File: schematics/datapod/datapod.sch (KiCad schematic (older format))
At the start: 5 parts, among them U1 ATmega328P-PU, Y1 16Mhz

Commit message: made 1st pcb
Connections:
- net VcR1: no longer names the net of RN1.10 (R10.1)
- no-connect marks 5 -> 6
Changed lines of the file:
@@
 Wire Wire Line
 	4200 6700 4550 6700
-Text GLabel 3600 6700 0    50   Input ~ 0
-VcR1
-Wire Wire Line
-	3600 6700 3800 6700
 Text GLabel 2450 1550 2    50   Input ~ 0
 MICRO_SD_CS
@@
 Connection ~ 4550 5900
 Connection ~ 4550 6000
+NoConn ~ 3800 6700
 $EndSCHEMATC

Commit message: added final routed PCB, gerbers and BOM
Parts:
- C1, C2: Part# (none) -> GJM0335C1HR22WB01D; part# GJM0335C1HR22WB01D -> (none)
- U1: Part# (none) -> 110-47-328-41-105000; Value2 110-47-328-41-105000 -> (none); Vendor microchip -> Digikey
- Y1: Part# (none) -> SER3686DKR-ND; part# SER3686DKR-ND -> (none)
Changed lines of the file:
@@
 F 2 "Package_DIP:DIP-28_W7.62mm_SMDSocket_SmallPads" H 1600 2550 50  0001 C CIN
 F 3 "http://ww1.microchip.com/downloads/en/DeviceDoc/ATmega328_P%20AVR%20MCU%20with%20picoPower%20Technology%20Data%20Sheet%2040001984A.pdf" H 1600 2550 50  0001 C CNN
-F 4 "microchip" H 1600 2550 50  0001 C CNN "Vendor"
-F 5 "110-47-328-41-105000 " H 1600 2550 50  0001 C CNN "Value2"
+F 4 "Digikey" H 1600 2550 50  0001 C CNN "Vendor"
+F 5 "110-47-328-41-105000 " H 1600 2550 50  0001 C CNN "Part#"
 F 6 "https://www.digikey.com/products/en?mpart=110-47-328-41-105000&v=54" H 1600 2550 50  0001 C CNN "Datasheet2"
 	1    1600 2550
@@
 F 4 "Digikey" H 4200 2150 50  0001 C CNN "Vendor"
 F 5 "https://www.digikey.com/product-detail/en/epson/FA-238-16.0000MB-C3/SER3686DKR-ND/2403540" H 4200 2150 50  0001 C CNN "extra"
-F 6 "SER3686DKR-ND" H 4200 2150 50  0001 C CNN "part#"
+F 6 "SER3686DKR-ND" H 4200 2150 50  0001 C CNN "Part#"
 	1    4200 2150
 	0    -1   -1   0
@@
 F 3 "https://search.murata.co.jp/Ceramy/image/img/A01X/G101/ENG/GJM0335C1HR22WB01-01.pdf" H 4200 1550 50  0001 C CNN
 F 4 "Digikey" H 4200 1550 50  0001 C CNN "Vendor"
-F 5 " GJM0335C1HR22WB01D" H 4200 1550 50  0001 C CNN "part#"
+F 5 " GJM0335C1HR22WB01D" H 4200 1550 50  0001 C CNN "Part#"
 	1    4200 1550
 	1    0    0    -1
@@
 F 3 "https://search.murata.co.jp/Ceramy/image/img/A01X/G101/ENG/GJM0335C1HR22WB01-01.pdf" H 4200 2750 50  0001 C CNN
 F 4 "Digikey" H 4200 2750 50  0001 C CNN "Vendor"
-F 5 " GJM0335C1HR22WB01D" H 4200 2750 50  0001 C CNN "part#"
+F 5 " GJM0335C1HR22WB01D" H 4200 2750 50  0001 C CNN "Part#"
 	1    4200 2750
 	1    0    0    -1

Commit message: restored lost changes... moving sd card reader and replacing rn2 with actual resistors
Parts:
- C1, C2: footprint Capacitor_SMD:C_0201_0603Metric -> Capacitor_SMD:C_1206_3216Metric_Pad1.42x1.75mm_HandSolder; Part# GJM0335C1HR22WB01D -> (none); part# (none) -> 399-9326-1-ND
- U1: symbol MCU_Microchip_ATmega:ATmega328P-PU -> datapod-rescue:ATmega328P-PU-MCU_Microchip_ATmega; Part# 110-47-328-41-105000 -> (none); Value2 (none) -> 110-47-328-41-105000; Vendor Digikey -> microchip
- Y1: Part# SER3686DKR-ND -> (none); part# (none) -> SER3686DKR-ND
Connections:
- net VcR1: now reaches RN1.10 (R10.1)
- no-connect marks 6 -> 5
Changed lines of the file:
@@
 EESchema Schematic File Version 4
-LIBS:datapod-cache
 EELAYER 30 0
 EELAYER END
@@
 $EndDescr
 $Comp
-L MCU_Microchip_ATmega:ATmega328P-PU U1
+L datapod-rescue:ATmega328P-PU-MCU_Microchip_ATmega U1
 U 1 1 5DBAFE2C
 P 1600 2550
@@
 F 2 "Package_DIP:DIP-28_W7.62mm_SMDSocket_SmallPads" H 1600 2550 50  0001 C CIN
 F 3 "http://ww1.microchip.com/downloads/en/DeviceDoc/ATmega328_P%20AVR%20MCU%20with%20picoPower%20Technology%20Data%20Sheet%2040001984A.pdf" H 1600 2550 50  0001 C CNN
-F 4 "Digikey" H 1600 2550 50  0001 C CNN "Vendor"
-F 5 "110-47-328-41-105000 " H 1600 2550 50  0001 C CNN "Part#"
+F 4 "microchip" H 1600 2550 50  0001 C CNN "Vendor"
+F 5 "110-47-328-41-105000 " H 1600 2550 50  0001 C CNN "Value2"
 F 6 "https://www.digikey.com/products/en?mpart=110-47-328-41-105000&v=54" H 1600 2550 50  0001 C CNN "Datasheet2"
 	1    1600 2550
@@
 F 4 "Digikey" H 4200 2150 50  0001 C CNN "Vendor"
 F 5 "https://www.digikey.com/product-detail/en/epson/FA-238-16.0000MB-C3/SER3686DKR-ND/2403540" H 4200 2150 50  0001 C CNN "extra"
-F 6 "SER3686DKR-ND" H 4200 2150 50  0001 C CNN "Part#"
+F 6 "SER3686DKR-ND" H 4200 2150 50  0001 C CNN "part#"
 	1    4200 2150
 	0    -1   -1   0
@@
 F 0 "C1" H 4300 1800 50  0000 L CNN
 F 1 "20pF" H 4300 1700 50  0000 L CNN
-F 2 "Capacitor_SMD:C_0201_0603Metric" H 4238 1400 50  0001 C CNN
-F 3 "https://search.murata.co.jp/Ceramy/image/img/A01X/G101/ENG/GJM0335C1HR22WB01-01.pdf" H 4200 1550 50  0001 C CNN
+F 2 "Capacitor_SMD:C_1206_3216Metric_Pad1.42x1.75mm_HandSolder" H 4238 1400 50  0001 C CNN
+F 3 "https://api.kemet.com/component-edge/download/datasheet/C1206C200K5GACTU.pdf" H 4200 1550 50  0001 C CNN
 F 4 "Digikey" H 4200 1550 50  0001 C CNN "Vendor"
-F 5 " GJM0335C1HR22WB01D" H 4200 1550 50  0001 C CNN "Part#"
+F 5 "399-9326-1-ND" H 4200 1550 50  0001 C CNN "part#"
 	1    4200 1550
-	1    0    0    -1
-$EndComp
-$Comp
-L Device:C C2
-U 1 1 5DBE647B
-P 4200 2750
-F 0 "C2" H 4315 2796 50  0000 L CNN
-F 1 "20pF" H 4315 2705 50  0000 L CNN
-F 2 "Capacitor_SMD:C_0201_0603Metric" H 4238 2600 50  0001 C CNN
-F 3 "https://search.murata.co.jp/Ceramy/image/img/A01X/G101/ENG/GJM0335C1HR22WB01-01.pdf" H 4200 2750 50  0001 C CNN
-F 4 "Digikey" H 4200 2750 50  0001 C CNN "Vendor"
-F 5 " GJM0335C1HR22WB01D" H 4200 2750 50  0001 C CNN "Part#"
-	1    4200 2750
 	1    0    0    -1
 $EndComp
@@
 $EndComp
 $Comp
-L power:GND #PWR03
+L power:GND #PWR0101
 U 1 1 5DC66802
 P 3850 2150
-F 0 "#PWR03" H 3850 1900 50  0001 C CNN
+F 0 "#PWR0101" H 3850 1900 50  0001 C CNN
 F 1 "GND" H 3855 1977 50  0000 C CNN
 F 2 "" H 3850 2150 50  0001 C CNN
@@
 $EndComp
 $Comp
-L power:GND #PWR04
+L power:GND #PWR0102
 U 1 1 5DC67152
 P 4600 2150
-F 0 "#PWR04" H 4600 1900 50  0001 C CNN
+F 0 "#PWR0102" H 4600 1900 50  0001 C CNN
 F 1 "GND" H 4605 1977 50  0000 C CNN
 F 2 "" H 4600 2150 50  0001 C CNN
@@
 	4000 2150 3850 2150
 $Comp
-L power:GND #PWR05
+L power:GND #PWR0103
 U 1 1 5DC89AE2
 P 4200 3050
-F 0 "#PWR05" H 4200 2800 50  0001 C CNN
+F 0 "#PWR0103" H 4200 2800 50  0001 C CNN
 F 1 "GND" H 4205 2877 50  0000 C CNN
 F 2 "" H 4200 3050 50  0001 C CNN
@@
 $EndComp
 $Comp
-L power:GND #PWR02
+L power:GND #PWR0104
 U 1 1 5DC8A1B9
 P 3950 1400
-F 0 "#PWR02" H 3950 1150 50  0001 C CNN
+F 0 "#PWR0104" H 3950 1150 50  0001 C CNN
 F 1 "GND" H 3955 1227 50  0000 C CNN
 F 2 "" H 3950 1400 50  0001 C CNN
@@
 Connection ~ 4200 1700
 $Comp
-L power:GND #PWR08
+L power:GND #PWR0105
 U 1 1 5DCB2EF6
 P 4550 6750
-F 0 "#PWR08" H 4550 6500 50  0001 C CNN
+F 0 "#PWR0105" H 4550 6500 50  0001 C CNN
 F 1 "GND" H 4555 6577 50  0000 C CNN
 F 2 "" H 4550 6750 50  0001 C CNN
@@
 	4200 6000 4550 6000
 $Comp
-L power:+5V #PWR07
+L power:+5V #PWR0106
 U 1 1 5DCB93CE
 P 4550 5550
-F 0 "#PWR07" H 4550 5400 50  0001 C CNN
+F 0 "#PWR0106" H 4550 5400 50  0001 C CNN
 F 1 "+5V" H 4565 5723 50  0000 C CNN
 F 2 "" H 4550 5550 50  0001 C CNN
@@
 Connection ~ 4550 5800
 $Comp
-L power:+5V #PWR01
+L power:+5V #PWR0107
 U 1 1 5DC99875
 P 1650 900
-F 0 "#PWR01" H 1650 750 50  0001 C CNN
+F 0 "#PWR0107" H 1650 750 50  0001 C CNN
 F 1 "+5V" H 1665 1073 50  0000 C CNN
 F 2 "" H 1650 900 50  0001 C CNN
@@
 	1650 1050 1700 1050
 $Comp
-L power:GND #PWR06
+L power:GND #PWR0108
 U 1 1 5DCA0B51
 P 1600 4050
-F 0 "#PWR06" H 1600 3800 50  0001 C CNN
+F 0 "#PWR0108" H 1600 3800 50  0001 C CNN
 F 1 "GND" H 1605 3877 50  0000 C CNN
 F 2 "" H 1600 4050 50  0001 C CNN
@@
 Wire Wire Line
 	3550 1700 4200 1700
-Connection ~ 4200 2600
 Wire Wire Line
 	2200 2050 3550 2050
@@
 Wire Wire Line
 	4200 6700 4550 6700
+Text GLabel 3600 6700 0    50   Input ~ 0
+VcR1
+Wire Wire Line
+	3600 6700 3800 6700
 Text GLabel 2450 1550 2    50   Input ~ 0
 MICRO_SD_CS
@@
 Connection ~ 4550 5900
 Connection ~ 4550 6000
-NoConn ~ 3800 6700
+$Comp
+L Device:C C2
+U 1 1 5DDB6B24
+P 4200 2750
+F 0 "C2" H 4300 3000 50  0000 L CNN
+F 1 "20pF" H 4300 2900 50  0000 L CNN
+F 2 "Capacitor_SMD:C_1206_3216Metric_Pad1.42x1.75mm_HandSolder" H 4238 2600 50  0001 C CNN
+F 3 "https://api.kemet.com/component-edge/download/datasheet/C1206C200K5GACTU.pdf" H 4200 2750 50  0001 C CNN
+F 4 "Digikey" H 4200 2750 50  0001 C CNN "Vendor"
+F 5 "399-9326-1-ND" H 4200 2750 50  0001 C CNN "part#"
+	1    4200 2750
+	1    0    0    -1
+$EndComp
+Connection ~ 4200 2600
 $EndSCHEMATC

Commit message: fixed bad gnd trace on 3.3v circuit and added comments to the silkscreen
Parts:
- added H1: MountingHole, datapod:MountingHole_0.4_inches_Pad_Via, symbol Mechanical:MountingHole
- added J9: Conn_02x03_Odd_Even, Connector_PinHeader_2.54mm:PinHeader_2x03_P2.54mm_Vertical_SMD, symbol Connector_Generic:Conn_02x03_Odd_Even
- added TP2: TestPoint_2Pole, TestPoint:TestPoint_2Pads_Pitch5.08mm_Drill1.3mm, symbol Connector:TestPoint_2Pole
- C1, C2: value 20pF -> 22pF; part# 399-9326-1-ND -> 399-8165-1-ND
- U1: symbol datapod-rescue:ATmega328P-PU-MCU_Microchip_ATmega -> MCU_Microchip_ATmega:ATmega328P-PU
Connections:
- net +5V: now also J9.2 (Pin_2)
- net GND: now also J9.6 (Pin_6), TP2.1, TP2.2
- net MICRO_SD_MISO: now also J9.1 (Pin_1)
- net MICRO_SD_MOSI: now also J9.4 (Pin_4)
- net MICRO_SD_SCK: now also J9.3 (Pin_3)
- net ~RESET: now also J9.5 (Pin_5)
- net VcR1: no longer names the net of RN1.10 (R10.1)
- no-connect marks 5 -> 6
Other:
- note added: "ICSP"
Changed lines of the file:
@@
 $EndDescr
-$Comp
-L datapod-rescue:ATmega328P-PU-MCU_Microchip_ATmega U1
-U 1 1 5DBAFE2C
-P 1600 2550
-F 0 "U1" H 1000 4500 50  0000 R CNN
-F 1 "ATmega328P-PU" H 1300 4300 50  0000 R CNN
-F 2 "Package_DIP:DIP-28_W7.62mm_SMDSocket_SmallPads" H 1600 2550 50  0001 C CIN
-F 3 "http://ww1.microchip.com/downloads/en/DeviceDoc/ATmega328_P%20AVR%20MCU%20with%20picoPower%20Technology%20Data%20Sheet%2040001984A.pdf" H 1600 2550 50  0001 C CNN
-F 4 "microchip" H 1600 2550 50  0001 C CNN "Vendor"
-F 5 "110-47-328-41-105000 " H 1600 2550 50  0001 C CNN "Value2"
-F 6 "https://www.digikey.com/products/en?mpart=110-47-328-41-105000&v=54" H 1600 2550 50  0001 C CNN "Datasheet2"
-	1    1600 2550
-	1    0    0    -1
-$EndComp
 $Comp
 L Device:Crystal_GND24 Y1
@@
 P 4200 1550
 F 0 "C1" H 4300 1800 50  0000 L CNN
-F 1 "20pF" H 4300 1700 50  0000 L CNN
+F 1 "22pF" H 4300 1700 50  0000 L CNN
 F 2 "Capacitor_SMD:C_1206_3216Metric_Pad1.42x1.75mm_HandSolder" H 4238 1400 50  0001 C CNN
-F 3 "https://api.kemet.com/component-edge/download/datasheet/C1206C200K5GACTU.pdf" H 4200 1550 50  0001 C CNN
+F 3 "https://api.kemet.com/component-edge/download/datasheet/C1206C220K2GACTU.pdf" H 4200 1550 50  0001 C CNN
 F 4 "Digikey" H 4200 1550 50  0001 C CNN "Vendor"
-F 5 "399-9326-1-ND" H 4200 1550 50  0001 C CNN "part#"
+F 5 "399-8165-1-ND" H 4200 1550 50  0001 C CNN "part#"
 	1    4200 1550
 	1    0    0    -1
@@
 	1    0    0    -1
 $EndComp
-Wire Wire Line
-	1600 1050 1650 1050
-Wire Wire Line
-	1650 900  1650 1050
-Connection ~ 1650 1050
-Wire Wire Line
-	1650 1050 1700 1050
 $Comp
 L power:GND #PWR0108
@@
 Wire Wire Line
 	4200 6700 4550 6700
-Text GLabel 3600 6700 0    50   Input ~ 0
-VcR1
-Wire Wire Line
-	3600 6700 3800 6700
 Text GLabel 2450 1550 2    50   Input ~ 0
 MICRO_SD_CS
@@
 P 4200 2750
 F 0 "C2" H 4300 3000 50  0000 L CNN
-F 1 "20pF" H 4300 2900 50  0000 L CNN
+F 1 "22pF" H 4300 2900 50  0000 L CNN
 F 2 "Capacitor_SMD:C_1206_3216Metric_Pad1.42x1.75mm_HandSolder" H 4238 2600 50  0001 C CNN
-F 3 "https://api.kemet.com/component-edge/download/datasheet/C1206C200K5GACTU.pdf" H 4200 2750 50  0001 C CNN
+F 3 "https://api.kemet.com/component-edge/download/datasheet/C1206C220K2GACTU.pdf" H 4200 2750 50  0001 C CNN
 F 4 "Digikey" H 4200 2750 50  0001 C CNN "Vendor"
-F 5 "399-9326-1-ND" H 4200 2750 50  0001 C CNN "part#"
+F 5 "399-8165-1-ND" H 4200 2750 50  0001 C CNN "part#"
 	1    4200 2750
 	1    0    0    -1
 $EndComp
 Connection ~ 4200 2600
+NoConn ~ 3800 6700
+$Comp
+L Mechanical:MountingHole H1
+U 1 1 5E1EDB2E
+P 3100 4800
+F 0 "H1" H 3200 4846 50  0000 L CNN
+F 1 "MountingHole" H 3200 4755 50  0000 L CNN
+F 2 "datapod:MountingHole_0.4_inches_Pad_Via" H 3100 4800 50  0001 C CNN
+F 3 "~" H 3100 4800 50  0001 C CNN
+	1    3100 4800
+	1    0    0    -1
+$EndComp
+$Comp
+L MCU_Microchip_ATmega:ATmega328P-PU U1
+U 1 1 5DBAFE2C
+P 1600 2550
+F 0 "U1" H 1000 4500 50  0000 R CNN
+F 1 "ATmega328P-PU" H 1300 4300 50  0000 R CNN
+F 2 "Package_DIP:DIP-28_W7.62mm_SMDSocket_SmallPads" H 1600 2550 50  0001 C CIN
+F 3 "http://ww1.microchip.com/downloads/en/DeviceDoc/ATmega328_P%20AVR%20MCU%20with%20picoPower%20Technology%20Data%20Sheet%2040001984A.pdf" H 1600 2550 50  0001 C CNN
+F 4 "microchip" H 1600 2550 50  0001 C CNN "Vendor"
+F 5 "110-47-328-41-105000 " H 1600 2550 50  0001 C CNN "Value2"
+F 6 "https://www.digikey.com/products/en?mpart=110-47-328-41-105000&v=54" H 1600 2550 50  0001 C CNN "Datasheet2"
+	1    1600 2550
+	1    0    0    -1
+$EndComp
+Wire Wire Line
+	1650 900  1650 1050
+Wire Wire Line
+	1650 1050 1600 1050
+Wire Wire Line
+	1650 1050 1700 1050
+Connection ~ 1650 1050
+$Comp
+L Connector_Generic:Conn_02x03_Odd_Even J9
+U 1 1 5E2206BC
+P 6300 1450
+F 0 "J9" H 6350 1767 50  0000 C CNN
+F 1 "Conn_02x03_Odd_Even" H 6350 1676 50  0000 C CNN
+F 2 "Connector_PinHeader_2.54mm:PinHeader_2x03_P2.54mm_Vertical_SMD" H 6300 1450 50  0001 C CNN
+F 3 "http://www.cnctech.us/pdfs/3020-XX-0300-00-TR.pdf" H 6300 1450 50  0001 C CNN
+F 4 "Digikey" H 6300 1450 50  0001 C CNN "Vendor"
+F 5 "1175-1864-ND" H 6300 1450 50  0001 C CNN "part#"
+	1    6300 1450
+	1    0    0    -1
+$EndComp
+Text GLabel 5850 1350 0    50   Input ~ 0
+MICRO_SD_MISO
+Text GLabel 5850 1450 0    50   Input ~ 0
+MICRO_SD_SCK
+Text GLabel 5850 1750 3    50   Input ~ 0
+~RESET
+Text GLabel 6800 1450 2    50   Input ~ 0
+MICRO_SD_MOSI
+Wire Wire Line
+	6100 1350 5850 1350
+Wire Wire Line
+	6100 1450 5850 1450
+Wire Wire Line
+	6600 1450 6800 1450
+Wire Wire Line
+	6100 1550 5850 1550
+Wire Wire Line
+	5850 1550 5850 1750
+$Comp
+L power:GND #PWR0110
+U 1 1 5E232FD1
+P 6800 1850
+F 0 "#PWR0110" H 6800 1600 50  0001 C CNN
+F 1 "GND" H 6805 1677 50  0000 C CNN
+F 2 "" H 6800 1850 50  0001 C CNN
+F 3 "" H 6800 1850 50  0001 C CNN
+	1    6800 1850
+	1    0    0    -1
+$EndComp
+Wire Wire Line
+	6600 1550 6800 1550
+Wire Wire Line
+	6800 1550 6800 1850
+$Comp
+L power:+5V #PWR0111
+U 1 1 5E236E01
+P 7000 1200
+F 0 "#PWR0111" H 7000 1050 50  0001 C CNN
+F 1 "+5V" H 7015 1373 50  0000 C CNN
+F 2 "" H 7000 1200 50  0001 C CNN
+F 3 "" H 7000 1200 50  0001 C CNN
+	1    7000 1200
+	1    0    0    -1
+$EndComp
+Wire Wire Line
+	6600 1350 7000 1350
+Wire Wire Line
+	7000 1350 7000 1200
+Text Notes 6300 1850 0    50   ~ 0
+ICSP
+$Comp
+L Connector:TestPoint_2Pole TP2
+U 1 1 5E27E889
+P 6400 3850
+F 0 "TP2" H 6400 4045 50  0000 C CNN
+F 1 "TestPoint_2Pole" H 6400 3954 50  0000 C CNN
+F 2 "TestPoint:TestPoint_2Pads_Pitch5.08mm_Drill1.3mm" H 6400 3850 50  0001 C CNN
+F 3 "~" H 6400 3850 50  0001 C CNN
+	1    6400 3850
+	1    0    0    -1
+$EndComp
+$Comp
+L power:GND #PWR02
+U 1 1 5E28008E
+P 6750 4300
+F 0 "#PWR02" H 6750 4050 50  0001 C CNN
+F 1 "GND" H 6755 4127 50  0000 C CNN
+F 2 "" H 6750 4300 50  0001 C CNN
+F 3 "" H 6750 4300 50  0001 C CNN
+	1    6750 4300
+	1    0    0    -1
+$EndComp
+Wire Wire Line
+	6750 3850 6750 4100
+Wire Wire Line
+	6200 3850 6200 4100
+Wire Wire Line
+	6200 4100 6750 4100
+Connection ~ 6750 4100
+Wire Wire Line
+	6750 4100 6750 4300
+Wire Wire Line
+	6600 3850 6750 3850
 $EndSCHEMATC

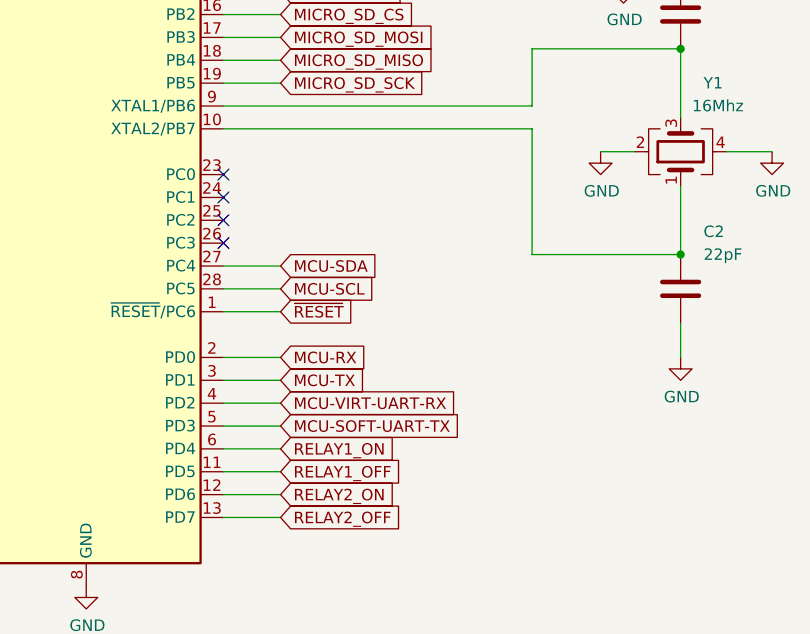
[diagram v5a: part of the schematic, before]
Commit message: added rtc stuff , rotated db9s , added on/off transistors for max chip and sdcard
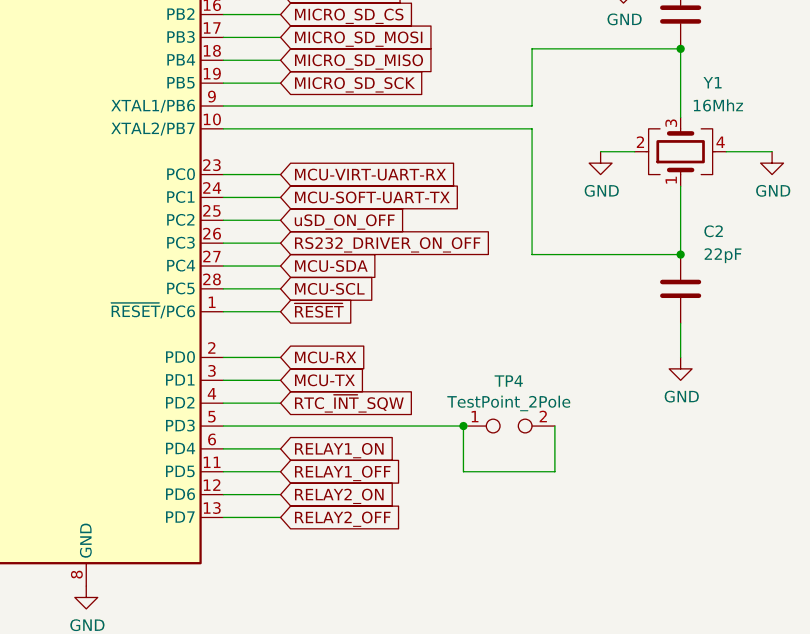
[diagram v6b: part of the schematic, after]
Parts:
- added TP4: TestPoint_2Pole, TestPoint:TestPoint_2Pads_Pitch5.08mm_Drill1.3mm, symbol Connector:TestPoint_2Pole
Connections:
- net MCU-SOFT-UART-TX: now also U1.24 (PC1); no longer U1.5 (PD3)
- net MCU-VIRT-UART-RX: now also U1.23 (PC0); no longer U1.4 (PD2)
- net uSD_ON_OFF: now reaches U1.25 (PC2)
- net RS232_DRIVER_ON_OFF: now reaches U1.26 (PC3)
- new net: TP4.1, TP4.2, U1.5 (PD3)
- new net RTC_~INT~_SQW: U1.4 (PD2)
- no-connect marks 6 -> 2
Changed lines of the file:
@@
 Wire Wire Line
 	2450 3150 2200 3150
-Text GLabel 2450 3250 2    50   Input ~ 0
+Text GLabel 2450 2250 2    50   Input ~ 0
 MCU-VIRT-UART-RX
-Wire Wire Line
-	2450 3250 2200 3250
-Text GLabel 2450 3350 2    50   Input ~ 0
+Text GLabel 2450 2350 2    50   Input ~ 0
 MCU-SOFT-UART-TX
-Wire Wire Line
-	2450 3350 2200 3350
 Text GLabel 2450 3450 2    50   Input ~ 0
 RELAY1_ON
@@
 F1 "datapod_rtc.sch" 50
 $EndSheet
-NoConn ~ 2200 2250
-NoConn ~ 2200 2350
-NoConn ~ 2200 2450
-NoConn ~ 2200 2550
 Wire Wire Line
 	4550 6100 4550 6000
@@
 Wire Wire Line
 	6600 3850 6750 3850
+Wire Wire Line
+	2200 2250 2450 2250
+Wire Wire Line
+	2200 2350 2450 2350
+Text GLabel 2450 3250 2    50   Input ~ 0
+RTC_~INT~_SQW
+Wire Wire Line
+	2200 3250 2450 3250
+Wire Wire Line
+	2200 2450 2450 2450
+Text GLabel 2450 2550 2    50   Input ~ 0
+RS232_DRIVER_ON_OFF
+Wire Wire Line
+	2200 2550 2450 2550
+Text GLabel 2450 2450 2    50   Input ~ 0
+uSD_ON_OFF
+$Comp
+L Connector:TestPoint_2Pole TP4
+U 1 1 5E2A98CD
+P 3450 3350
+F 0 "TP4" H 3450 3545 50  0000 C CNN
+F 1 "TestPoint_2Pole" H 3450 3454 50  0000 C CNN
+F 2 "TestPoint:TestPoint_2Pads_Pitch5.08mm_Drill1.3mm" H 3450 3350 50  0001 C CNN
+F 3 "~" H 3450 3350 50  0001 C CNN
+	1    3450 3350
+	1    0    0    -1
+$EndComp
+Wire Wire Line
+	2200 3350 3250 3350
+Wire Wire Line
+	3250 3350 3250 3550
+Wire Wire Line
+	3250 3550 3650 3550
+Wire Wire Line
+	3650 3550 3650 3350
+Connection ~ 3250 3350
 $EndSCHEMATC

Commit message: rev 3 , moved db9 connectors out and added ajumper to change output to 14.4v
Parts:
- C1, C2: Part# (none) -> 399-8165-1-ND; part# 399-8165-1-ND -> (none)
- H1, TP2, TP4: Part# (none) -> DNI
- J9: Part# (none) -> WM17457-ND; part# 1175-1864-ND -> (none)
- U1: Datasheet2 https://www.digikey.com/products/en?mpart=110-47-328-41-105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 -> (none); Part# (none) -> 110-47-328-41-105000; Part#-2 (none) -> ATmega328P-U; Value2 110-47-328-41-105000 -> (none); Vendor microchip -> Digikey
- Y1: Part# (none) -> SER3686DKR-ND; extra https://www.digikey.com/product-detail/en/epson/FA-238-16.0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 -> (none); part# SER3686DKR-ND -> (none)
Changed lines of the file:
@@
 F 3 "https://support.epson.biz/td/api/doc_check.php?dl=brief_FA-238&lang=en" H 4200 2150 50  0001 C CNN
 F 4 "Digikey" H 4200 2150 50  0001 C CNN "Vendor"
-F 5 "https://www.digikey.com/product-detail/en/epson/FA-238-16.0000MB-C3/SER3686DKR-ND/2403540" H 4200 2150 50  0001 C CNN "extra"
-F 6 "SER3686DKR-ND" H 4200 2150 50  0001 C CNN "part#"
+F 5 "SER3686DKR-ND" H 4200 2150 50  0001 C CNN "Part#"
 	1    4200 2150
 	0    -1   -1   0
@@
 F 3 "https://api.kemet.com/component-edge/download/datasheet/C1206C220K2GACTU.pdf" H 4200 1550 50  0001 C CNN
 F 4 "Digikey" H 4200 1550 50  0001 C CNN "Vendor"
-F 5 "399-8165-1-ND" H 4200 1550 50  0001 C CNN "part#"
+F 5 "399-8165-1-ND" H 4200 1550 50  0001 C CNN "Part#"
 	1    4200 1550
 	1    0    0    -1
@@
 F 3 "https://api.kemet.com/component-edge/download/datasheet/C1206C220K2GACTU.pdf" H 4200 2750 50  0001 C CNN
 F 4 "Digikey" H 4200 2750 50  0001 C CNN "Vendor"
-F 5 "399-8165-1-ND" H 4200 2750 50  0001 C CNN "part#"
+F 5 "399-8165-1-ND" H 4200 2750 50  0001 C CNN "Part#"
 	1    4200 2750
 	1    0    0    -1
@@
 F 2 "datapod:MountingHole_0.4_inches_Pad_Via" H 3100 4800 50  0001 C CNN
 F 3 "~" H 3100 4800 50  0001 C CNN
+F 4 "DNI" H 3100 4800 50  0001 C CNN "Part#"
 	1    3100 4800
 	1    0    0    -1
@@
 F 2 "Package_DIP:DIP-28_W7.62mm_SMDSocket_SmallPads" H 1600 2550 50  0001 C CIN
 F 3 "http://ww1.microchip.com/downloads/en/DeviceDoc/ATmega328_P%20AVR%20MCU%20with%20picoPower%20Technology%20Data%20Sheet%2040001984A.pdf" H 1600 2550 50  0001 C CNN
-F 4 "microchip" H 1600 2550 50  0001 C CNN "Vendor"
-F 5 "110-47-328-41-105000 " H 1600 2550 50  0001 C CNN "Value2"
-F 6 "https://www.digikey.com/products/en?mpart=110-47-328-41-105000&v=54" H 1600 2550 50  0001 C CNN "Datasheet2"
+F 4 "Digikey" H 1600 2550 50  0001 C CNN "Vendor"
+F 5 "110-47-328-41-105000 " H 1600 2550 50  0001 C CNN "Part#"
+F 6 "ATmega328P-U" H 1600 2550 50  0001 C CNN "Part#-2"
 	1    1600 2550
 	1    0    0    -1
@@
 F 1 "Conn_02x03_Odd_Even" H 6350 1676 50  0000 C CNN
 F 2 "Connector_PinHeader_2.54mm:PinHeader_2x03_P2.54mm_Vertical_SMD" H 6300 1450 50  0001 C CNN
-F 3 "http://www.cnctech.us/pdfs/3020-XX-0300-00-TR.pdf" H 6300 1450 50  0001 C CNN
+F 3 "https://www.molex.com/pdm_docs/sd/015910060_sd.pdf" H 6300 1450 50  0001 C CNN
 F 4 "Digikey" H 6300 1450 50  0001 C CNN "Vendor"
-F 5 "1175-1864-ND" H 6300 1450 50  0001 C CNN "part#"
+F 5 "WM17457-ND" H 6300 1450 50  0001 C CNN "Part#"
 	1    6300 1450
 	1    0    0    -1
@@
 F 2 "TestPoint:TestPoint_2Pads_Pitch5.08mm_Drill1.3mm" H 6400 3850 50  0001 C CNN
 F 3 "~" H 6400 3850 50  0001 C CNN
+F 4 "DNI" H 6400 3850 50  0001 C CNN "Part#"
 	1    6400 3850
 	1    0    0    -1
@@
 F 2 "TestPoint:TestPoint_2Pads_Pitch5.08mm_Drill1.3mm" H 3450 3350 50  0001 C CNN
 F 3 "~" H 3450 3350 50  0001 C CNN
+F 4 "DNI" H 3450 3350 50  0001 C CNN "Part#"
 	1    3450 3350
 	1    0    0    -1
